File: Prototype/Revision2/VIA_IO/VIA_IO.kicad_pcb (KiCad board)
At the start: 2 copper layers, 100.2 x 88.2 mm, 88 parts, among them CN8 CONTROL_PORT, J10 VIA, J12 VIC, J18 3V3, J19 +5V, J21 JOY_POTS, J22 JOY_POTS, J23 JOY_PORT, J24 JOY_PORT, J25 SYNC, J4 KEYBOARD, J5 MOTOR, J6 9VAC, J8 EDGE, SW1 POWER_SWITCH, U1 BD60GC0WEFJ-E2, U12 THS7316D, U15 74LVC1G06, U17 74LVC1G06, U18 74LVC1G06, U19 74LVC1G06, U28 TLV74333PDBVR, U32 LM1881, U7 6522 VIA, U8 6522 VIA

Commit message: - Added the prototype rev2 IO Board schematic.
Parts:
- removed the C10 at (232.7, 81.5)
- removed the C11 at (232.7, 84.0)
- removed the C12 at (232.7, 86.5)
- removed the C35 at (126.3, 63.3)
- removed the C49 at (159.4, 55.9)
- removed the C50 at (157.6, 67.6)
- removed the C51 at (73.9, 116.6)
- removed C80: 4.7uf, Capacitor_SMD:C_0603_1608Metric
- removed C83, C84: 1nf, Capacitor_SMD:C_0603_1608Metric
- removed the C9 at (232.7, 78.9)
- removed J12: VIC, Connector_PinHeader_2.54mm:PinHeader_1x03_P2.54mm_Vertical
- removed J18: 3V3, Connector_PinHeader_2.54mm:PinHeader_1x03_P2.54mm_Vertical
- removed J19: +5V, Connector_PinHeader_2.54mm:PinHeader_2x04_P2.54mm_Vertical
- removed J21, J22: JOY_POTS, Connector_PinHeader_2.54mm:PinHeader_1x03_P2.54mm_Vertical
- removed J23, J24: JOY_PORT, Dave Footprints:JOYPORT_9PIN_HEADER
- removed J25: SYNC, Connector_PinHeader_2.54mm:PinHeader_1x04_P2.54mm_Vertical
- removed Power2: POWER, LED_SMD:LED_0805_2012Metric
- removed U19: 74LVC1G06, Package_TO_SOT_SMD:SOT-353_SC-70-5
- removed U28: TLV74333PDBVR, Package_TO_SOT_SMD:SOT-23-5
- added C1: 100nf, Capacitor_SMD:C_0603_1608Metric, F.Cu at (47.2, 101.6)
- added C16: 100nf, Capacitor_SMD:C_0603_1608Metric, F.Cu at (213.4, 56.0)
- added C17: 4.7uf, Capacitor_SMD:C_0603_1608Metric, F.Cu at (49.0, 60.9)
- added C18: 100nf, Capacitor_SMD:C_0603_1608Metric, F.Cu at (49.8, 128.6)
- added C19: 100nf, Capacitor_SMD:C_0603_1608Metric, F.Cu at (245.1, 31.8)
- added C2: 100nf, Capacitor_SMD:C_0603_1608Metric, F.Cu at (40.6, 114.1)
- added C20: 100nf, Capacitor_SMD:C_0603_1608Metric, F.Cu at (245.1, 26.8)
- added C21: 100nf, Capacitor_SMD:C_0603_1608Metric, F.Cu at (260.2, 84.9)
- added C22: 100nf, Capacitor_SMD:C_0603_1608Metric, F.Cu at (174.8, 28.9)
- added C23: 100nf, Capacitor_SMD:C_0603_1608Metric, F.Cu at (174.8, 34.0)
- added C24: 100nf, Capacitor_SMD:C_0603_1608Metric, F.Cu at (52.2, 71.0)
- added C25: 100nf, Capacitor_SMD:C_0603_1608Metric, F.Cu at (245.1, 34.3)
- added C26: 100nf, Capacitor_SMD:C_0603_1608Metric, F.Cu at (245.1, 29.3)
- added C27: 100nf, Capacitor_SMD:C_0603_1608Metric, F.Cu at (260.2, 87.4)
- added C29: 100nf, Capacitor_SMD:C_0603_1608Metric, F.Cu at (174.8, 36.5)
- added C3: 100nf, Capacitor_SMD:C_0603_1608Metric, F.Cu at (40.6, 106.6)
- added C30: 1nf, Capacitor_SMD:C_0603_1608Metric, F.Cu at (180.5, 96.1)
- added C31: 100nf, Capacitor_SMD:C_0603_1608Metric, F.Cu at (46.6, 107.8)
- added C32: 1nf, Capacitor_SMD:C_0603_1608Metric, F.Cu at (180.5, 93.6)
- added C33: 100nf, Capacitor_SMD:C_0603_1608Metric, F.Cu at (160.8, 158.4)
- added C34: 100nf, Capacitor_SMD:C_0603_1608Metric, F.Cu at (174.8, 26.4)
- added C36: 100nf, Capacitor_SMD:C_0603_1608Metric, F.Cu at (46.6, 110.3)
- added C38: 100nf, Capacitor_SMD:C_0603_1608Metric, F.Cu at (46.6, 112.8)
- added C39: 100nf, Capacitor_SMD:C_0603_1608Metric, F.Cu at (17.9, 0.72)
- added C4: 100nf, Capacitor_SMD:C_0603_1608Metric, F.Cu at (47.2, 99.1)
- added C40: 100nf, Capacitor_SMD:C_0603_1608Metric, F.Cu at (17.9, 3.23)
- added C42: 510pf, Capacitor_SMD:C_0603_1608Metric, F.Cu at (17.9, 15.8)
- added C43: 10pf, Capacitor_SMD:C_0603_1608Metric, F.Cu at (17.9, 5.75)
- added C45: 100nf, Capacitor_SMD:C_0603_1608Metric, F.Cu at (17.9, 13.3)
- added C46: 4.7uf, Capacitor_SMD:C_0603_1608Metric, F.Cu at (17.9, 10.8)
- added C48: 100nf, Capacitor_SMD:C_0603_1608Metric, F.Cu at (17.9, 8.26)
- added C5: 100nf, Capacitor_SMD:C_0603_1608Metric, F.Cu at (40.6, 111.6)
- added C54: 4.7uf, Capacitor_SMD:C_0603_1608Metric, F.Cu at (21.9, 0.72)
- added C55: 100nf, Capacitor_SMD:C_0603_1608Metric, F.Cu at (98.0, 77.5)
- added C57: 100nf, Capacitor_SMD:C_0603_1608Metric, F.Cu at (264.4, 97.9)
- added C58: 100nf, Capacitor_SMD:C_0603_1608Metric, F.Cu at (21.9, 3.23)
- added C59: 100nf, Capacitor_SMD:C_0603_1608Metric, F.Cu at (21.9, 5.75)
- added C6: 100nf, Capacitor_SMD:C_0603_1608Metric, F.Cu at (40.6, 109.1)
- added C60: 100nf, Capacitor_SMD:C_0603_1608Metric, F.Cu at (21.9, 8.26)
- added C61: 100nf, Capacitor_SMD:C_0603_1608Metric, F.Cu at (52.2, 87.6)
- added C62: 100nf, Capacitor_SMD:C_0603_1608Metric, F.Cu at (21.9, 10.8)
- added C63: 100nf, Capacitor_SMD:C_0603_1608Metric, F.Cu at (190.6, 109.0)
- added C64: 100nf, Capacitor_SMD:C_0603_1608Metric, F.Cu at (213.4, 58.5)
- added C65: 100nf, Capacitor_SMD:C_0603_1608Metric, F.Cu at (213.4, 61.0)
- added C66: 4.7uf, Capacitor_SMD:C_0603_1608Metric, F.Cu at (213.4, 63.5)
- added C67: 100nf, Capacitor_SMD:C_0603_1608Metric, F.Cu at (213.4, 66.0)
- added C68: 4.7uf, Capacitor_SMD:C_0603_1608Metric, F.Cu at (213.4, 68.5)
- added C69: 100nf, Capacitor_SMD:C_0603_1608Metric, F.Cu at (217.5, 56.0)
- added C7: 100nf, Capacitor_SMD:C_0603_1608Metric, F.Cu at (47.2, 96.6)
- added C70: 100nf, Capacitor_SMD:C_0603_1608Metric, F.Cu at (26.0, 157.0)
- added C71: 100nf, Capacitor_SMD:C_0603_1608Metric, F.Cu at (26.0, 159.5)
- added CDone1: DONE, LED_SMD:LED_0805_2012Metric, F.Cu at (200.1, 74.7)
- added D1: B140-E3, Diode_SMD:D_SOD-123, F.Cu at (161.7, 155.5)
- added D10: D_Dual_Series_ACK, Package_TO_SOT_SMD:SOT-23, F.Cu at (166.9, 80.9)
- added D2: ESDA6V1SC5, _Custom:SOT-553, B.Cu at (131.0, 136.3)
- added D4: ESDA6V1SC5, _Custom:SOT-553, F.Cu at (35.1, 179.6)
- added D5: ESDA6V1SC5, _Custom:SOT-553, F.Cu at (195.4, 75.4)
- added D6: ESDA6V1SC5, _Custom:SOT-553, F.Cu at (174.3, 121.7)
- added D7: ESDA6V1SC5, _Custom:SOT-553, F.Cu at (174.3, 124.8)
- added D8: ESDA6V1SC5, _Custom:SOT-553, F.Cu at (174.3, 128.0)
- added D9: ESDA6V1SC5, _Custom:SOT-553, F.Cu at (166.9, 77.7)
- added J1: +5V, Connector_PinHeader_2.54mm:PinHeader_2x04_P2.54mm_Vertical, F.Cu at (154.0, 156.1)
- added J10: DV INTERCONNECT, Connector_PinHeader_2.54mm:PinHeader_2x05_P2.54mm_Vertical, F.Cu at (1.79, 1.79)
- added J2: JOY_POTS, Connector_PinHeader_2.54mm:PinHeader_1x03_P2.54mm_Vertical, F.Cu at (176.2, 92.1)
- added J3: KEYBOARD, _Custom:CON_VIC20_KEYBOARD, F.Cu at (64.8, 131.8)
- added J7: USB_B_Micro, _Custom:USB_Micro-B_Amphenol_10103594-0001LF_Horizontal, F.Cu at (28.7, 177.2)
- added J9: HDMI, Connector_Video:HDMI_A_Amphenol_10029449-x01xLF_Horizontal, F.Cu at (156.5, 122.0)
- added JP1: SolderJumper_2_Bridged, Jumper:SolderJumper-2_P1.3mm_Bridged_RoundedPad1.0x1.5mm, F.Cu at (161.0, 167.0)
- added JP2: SolderJumper_2_Bridged, Jumper:SolderJumper-2_P1.3mm_Bridged_RoundedPad1.0x1.5mm, F.Cu at (254.9, 72.8)
- added Je1: BOOT SEL, Connector_PinHeader_2.54mm:PinHeader_1x02_P2.54mm_Vertical, F.Cu at (47.6, 10.3)
- added Power1: POWER, LED_SMD:LED_0805_2012Metric, F.Cu at (161.1, 163.7)
- added Q1: 2SC2712-GR,LF, Package_TO_SOT_SMD:TSOT-23, F.Cu at (102.7, 78.4)
- added R1: 1k, Resistor_SMD:R_0603_1608Metric, F.Cu at (160.8, 160.9)
- added R10: 4k7, Resistor_SMD:R_0603_1608Metric, F.Cu at (22.4, 48.5)
- added R102: 470, Resistor_SMD:R_0603_1608Metric, F.Cu at (33.9, 13.3)
- added R103: 1k, Resistor_SMD:R_0603_1608Metric, F.Cu at (33.9, 15.8)
- added R104: 1k, Resistor_SMD:R_0603_1608Metric, F.Cu at (25.9, 0.72)
- added R105: 27R, Resistor_SMD:R_0603_1608Metric, F.Cu at (21.9, 13.3)
- added R106: 27R, Resistor_SMD:R_0603_1608Metric, F.Cu at (25.9, 3.23)
- added R107: 27R, Resistor_SMD:R_0603_1608Metric, F.Cu at (21.9, 18.3)
- added R108: 27R, Resistor_SMD:R_0603_1608Metric, F.Cu at (60.6, 37.5)
- added R109: 27R, Resistor_SMD:R_0603_1608Metric, F.Cu at (98.0, 79.4)
- added R11: 4k7, Resistor_SMD:R_0603_1608Metric, F.Cu at (22.4, 51.0)
- added R110: 27R, Resistor_SMD:R_0603_1608Metric, F.Cu at (260.2, 102.5)
- added R111: 27R, Resistor_SMD:R_0603_1608Metric, F.Cu at (260.2, 100.0)
- added R112: 10k, Resistor_SMD:R_0603_1608Metric, F.Cu at (143.8, 123.7)
- added R113: 10k, Resistor_SMD:R_0603_1608Metric, F.Cu at (143.8, 125.1)
- added R114: 10k, Resistor_SMD:R_0603_1608Metric, F.Cu at (143.8, 120.8)
- added R115: 0R, Resistor_SMD:R_0603_1608Metric, F.Cu at (143.8, 122.2)
- added R116: 0R, Resistor_SMD:R_0603_1608Metric, F.Cu at (143.8, 117.8)
- added R117: 0R, Resistor_SMD:R_0603_1608Metric, F.Cu at (143.8, 119.3)
- added R118: 0R, Resistor_SMD:R_0603_1608Metric, F.Cu at (143.8, 114.9)
- added R119: 0R, Resistor_SMD:R_0603_1608Metric, F.Cu at (143.8, 116.4)
- added R12: 4k7, Resistor_SMD:R_0603_1608Metric, F.Cu at (22.4, 53.5)
- added R120: 0R, Resistor_SMD:R_0603_1608Metric, F.Cu at (217.5, 61.0)
- added R121: 0R, Resistor_SMD:R_0603_1608Metric, F.Cu at (217.5, 63.5)
- added R122: 0R, Resistor_SMD:R_0603_1608Metric, F.Cu at (21.9, 15.8)
- added R123: 0R, Resistor_SMD:R_0603_1608Metric, F.Cu at (217.5, 66.0)
- added R124: 0R, Resistor_SMD:R_0603_1608Metric, F.Cu at (26.0, 162.0)
- added R125: 0R, Resistor_SMD:R_0603_1608Metric, F.Cu at (26.0, 164.5)
- added R126: 0R, Resistor_SMD:R_0603_1608Metric, F.Cu at (26.0, 167.0)
- added R127: 0R, Resistor_SMD:R_0603_1608Metric, F.Cu at (26.0, 169.5)
- added R128: 0R, Resistor_SMD:R_0603_1608Metric, F.Cu at (26.0, 172.0)
- added R129: 0R, Resistor_SMD:R_0603_1608Metric, F.Cu at (30.0, 157.0)
- added R13: 4k7, Resistor_SMD:R_0603_1608Metric, F.Cu at (22.4, 56.0)
- added R130: 0R, Resistor_SMD:R_0603_1608Metric, F.Cu at (30.0, 159.5)
- added R131: 0R, Resistor_SMD:R_0603_1608Metric, F.Cu at (30.0, 162.0)
- added R132: 10k, Resistor_SMD:R_0603_1608Metric, F.Cu at (30.0, 164.5)
- added R133: 10k, Resistor_SMD:R_0603_1608Metric, F.Cu at (30.0, 167.0)
- added R134: 10k, Resistor_SMD:R_0603_1608Metric, F.Cu at (30.0, 169.5)
- added R135: 10k, Resistor_SMD:R_0603_1608Metric, F.Cu at (30.0, 172.0)
- added R136: 10k, Resistor_SMD:R_0603_1608Metric, F.Cu at (34.0, 157.0)
- added R137: 10k, Resistor_SMD:R_0603_1608Metric, F.Cu at (34.0, 159.5)
- added R138: 2k2, Resistor_SMD:R_0603_1608Metric, F.Cu at (34.0, 162.0)
- added R139: 220, Resistor_SMD:R_0603_1608Metric, F.Cu at (34.0, 164.5)
- added R14: 4k7, Resistor_SMD:R_0603_1608Metric, F.Cu at (22.4, 58.6)
- added R140: 220, Resistor_SMD:R_0603_1608Metric, F.Cu at (34.0, 167.0)
- added R141: 220, Resistor_SMD:R_0603_1608Metric, F.Cu at (34.0, 169.5)
- added R142: 220, Resistor_SMD:R_0603_1608Metric, F.Cu at (34.0, 172.0)
- added R143: 220, Resistor_SMD:R_0603_1608Metric, F.Cu at (38.0, 157.0)
- added R144: 220, Resistor_SMD:R_0603_1608Metric, F.Cu at (38.0, 159.5)
- added R145: 220, Resistor_SMD:R_0603_1608Metric, F.Cu at (38.0, 162.0)
- added R146: 220, Resistor_SMD:R_0603_1608Metric, F.Cu at (38.0, 164.5)
- added R147: 10k, Resistor_SMD:R_0603_1608Metric, F.Cu at (38.0, 167.0)
- added R148: 27R, Resistor_SMD:R_0603_1608Metric, F.Cu at (38.0, 169.5)
- added R15: 4k7, Resistor_SMD:R_0603_1608Metric, F.Cu at (22.4, 61.1)
- added R16: 4k7, Resistor_SMD:R_0603_1608Metric, F.Cu at (26.4, 48.5)
- added R17: 4k7, Resistor_SMD:R_0603_1608Metric, F.Cu at (26.4, 51.0)
- added R18: 4k7, Resistor_SMD:R_0603_1608Metric, F.Cu at (44.2, 76.6)
- added R19: 4k7, Resistor_SMD:R_0603_1608Metric, F.Cu at (44.2, 79.2)
- added R20: 4k7, Resistor_SMD:R_0603_1608Metric, F.Cu at (44.2, 81.7)
- added R21: 4k7, Resistor_SMD:R_0603_1608Metric, F.Cu at (60.6, 34.9)
- added R22: 4k7, Resistor_SMD:R_0603_1608Metric, F.Cu at (37.4, 76.9)
- added R23: 4k7, Resistor_SMD:R_0603_1608Metric, F.Cu at (44.2, 84.2)
- added R24: 4k7, Resistor_SMD:R_0603_1608Metric, F.Cu at (44.2, 86.7)
- added R25: 4k7, Resistor_SMD:R_0603_1608Metric, F.Cu at (44.2, 89.2)
- added R26: 4k7, Resistor_SMD:R_0603_1608Metric, F.Cu at (174.8, 41.5)
- added R27: 4k7, Resistor_SMD:R_0603_1608Metric, F.Cu at (174.8, 44.0)
- added R28: 4k7, Resistor_SMD:R_0603_1608Metric, F.Cu at (174.8, 46.5)
- added R29: 4k7, Resistor_SMD:R_0603_1608Metric, F.Cu at (178.8, 26.4)
- added R3: 4k7, Resistor_SMD:R_0603_1608Metric, F.Cu at (26.4, 56.0)
- added R30: 4k7, Resistor_SMD:R_0603_1608Metric, F.Cu at (178.8, 28.9)
- added R31: 4k7, Resistor_SMD:R_0603_1608Metric, F.Cu at (178.8, 31.5)
- added R32: 4k7, Resistor_SMD:R_0603_1608Metric, F.Cu at (178.8, 34.0)
- added R33: 4k7, Resistor_SMD:R_0603_1608Metric, F.Cu at (178.8, 36.5)
- added R34: 4k7, Resistor_SMD:R_0603_1608Metric, F.Cu at (178.8, 39.0)
- added R35: 4k7, Resistor_SMD:R_0603_1608Metric, F.Cu at (178.8, 41.5)
- added R36: 4k7, Resistor_SMD:R_0603_1608Metric, F.Cu at (178.8, 44.0)
- added R37: 4k7, Resistor_SMD:R_0603_1608Metric, F.Cu at (178.8, 46.5)
- added R4: 4k7, Resistor_SMD:R_0603_1608Metric, F.Cu at (26.4, 58.6)
- added R42: 200k, Resistor_SMD:R_0603_1608Metric, F.Cu at (245.1, 39.3)
- added R43: 200k, Resistor_SMD:R_0603_1608Metric, F.Cu at (245.1, 36.8)
- added R44: 200k, Resistor_SMD:R_0603_1608Metric, F.Cu at (260.2, 95.0)
- added R45: 200k, Resistor_SMD:R_0603_1608Metric, F.Cu at (182.8, 36.5)
- added R46: 200k, Resistor_SMD:R_0603_1608Metric, F.Cu at (182.8, 39.0)
- added R47: 10k, Resistor_SMD:R_0603_1608Metric, F.Cu at (37.4, 81.9)
- added R48: 2k2, Resistor_SMD:R_0603_1608Metric, F.Cu at (103.1, 145.1)
- added R49: 2k2, Resistor_SMD:R_0603_1608Metric, F.Cu at (138.6, 127.9)
- added R5: 4k7, Resistor_SMD:R_0603_1608Metric, F.Cu at (26.4, 61.1)
- added R50: 2k2, Resistor_SMD:R_0603_1608Metric, F.Cu at (136.5, 129.6)
- added R51: 2k2, Resistor_SMD:R_0603_1608Metric, F.Cu at (137.1, 133.7)
- added R52: 2k2, Resistor_SMD:R_0603_1608Metric, B.Cu at (129.6, 129.6)
- added R53: 2k2, Resistor_SMD:R_0603_1608Metric, B.Cu at (125.2, 131.4)
- added R54: 2k2, Resistor_SMD:R_0603_1608Metric, F.Cu at (98.0, 145.6)
- added R55: 2k2, Resistor_SMD:R_0603_1608Metric, F.Cu at (93.5, 146.5)
- added R56: 2k2, Resistor_SMD:R_0603_1608Metric, B.Cu at (121.8, 133.2)
- added R57: 2k2, Resistor_SMD:R_0603_1608Metric, B.Cu at (125.2, 132.9)
- added R58: 2k2, Resistor_SMD:R_0603_1608Metric, B.Cu at (129.6, 131.1)
- added R59: 2k2, Resistor_SMD:R_0603_1608Metric, B.Cu at (130.8, 152.4)
- added R6: 4k7, Resistor_SMD:R_0603_1608Metric, F.Cu at (30.4, 48.5)
- added R60: 2k2, Resistor_SMD:R_0603_1608Metric, B.Cu at (133.3, 152.4)
- added R61: 2k2, Resistor_SMD:R_0603_1608Metric, B.Cu at (143.8, 134.9)
- added R62: 2k2, Resistor_SMD:R_0603_1608Metric, F.Cu at (142.5, 129.3)
- added R63: 2k2, Resistor_SMD:R_0603_1608Metric, F.Cu at (144.1, 129.3)
- added R64: 2k2, Resistor_SMD:R_0603_1608Metric, F.Cu at (18.4, 48.5)
- added R65: 2k2, Resistor_SMD:R_0603_1608Metric, F.Cu at (18.4, 51.0)
- added R66: 2k2, Resistor_SMD:R_0603_1608Metric, F.Cu at (18.4, 53.5)
- added R67: 2k2, Resistor_SMD:R_0603_1608Metric, F.Cu at (60.6, 32.4)
- added R68: 2k2, Resistor_SMD:R_0603_1608Metric, F.Cu at (37.4, 79.4)
- added R69: 2k2, Resistor_SMD:R_0603_1608Metric, F.Cu at (18.4, 56.0)
- added R7: 4k7, Resistor_SMD:R_0603_1608Metric, F.Cu at (30.4, 51.0)
- added R70: 2k2, Resistor_SMD:R_0603_1608Metric, F.Cu at (18.4, 58.6)
- added R71: 2k2, Resistor_SMD:R_0603_1608Metric, F.Cu at (18.4, 61.1)
- added R72: 2k2, Resistor_SMD:R_0603_1608Metric, F.Cu at (182.8, 41.5)
- added R74: 2k2, Resistor_SMD:R_0603_1608Metric, F.Cu at (182.8, 46.5)
- added R75: 2k2, Resistor_SMD:R_0603_1608Metric, F.Cu at (186.8, 26.4)
- added R76: 2k2, Resistor_SMD:R_0603_1608Metric, F.Cu at (186.8, 28.9)
- added R77: 2k2, Resistor_SMD:R_0603_1608Metric, F.Cu at (186.8, 31.5)
- added R78: 2k2, Resistor_SMD:R_0603_1608Metric, F.Cu at (186.8, 34.0)
- added R79: 2k2, Resistor_SMD:R_0603_1608Metric, F.Cu at (186.8, 36.5)
- added R8: 4k7, Resistor_SMD:R_0603_1608Metric, F.Cu at (30.4, 53.5)
- added R80: 2k2, Resistor_SMD:R_0603_1608Metric, F.Cu at (186.8, 39.0)
- added R81: 2k2, Resistor_SMD:R_0603_1608Metric, F.Cu at (186.8, 41.5)
- added R82: 2k2, Resistor_SMD:R_0603_1608Metric, F.Cu at (186.8, 44.0)
- added R83: 2k2, Resistor_SMD:R_0603_1608Metric, F.Cu at (186.8, 46.5)
- added R84: 2k2, Resistor_SMD:R_0603_1608Metric, F.Cu at (190.8, 26.4)
- added R85: 2k2, Resistor_SMD:R_0603_1608Metric, F.Cu at (190.8, 28.9)
- added R86: 2k2, Resistor_SMD:R_0603_1608Metric, F.Cu at (190.8, 31.5)
- added R87: 2k2, Resistor_SMD:R_0603_1608Metric, F.Cu at (190.8, 34.0)
- added R88: 10k, Resistor_SMD:R_0603_1608Metric, F.Cu at (174.8, 39.0)
- added R9: 4k7, Resistor_SMD:R_0603_1608Metric, F.Cu at (30.4, 56.0)
- added R90: 1K, Resistor_SMD:R_0603_1608Metric, F.Cu at (29.9, 0.72)
- added R91: 1K, Resistor_SMD:R_0603_1608Metric, F.Cu at (33.9, 3.23)
- added R92: 620R, Resistor_SMD:R_0603_1608Metric, F.Cu at (33.9, 5.75)
- added R93: 680k, Resistor_SMD:R_0603_1608Metric, F.Cu at (33.9, 8.26)
- added R94: 75, Resistor_SMD:R_0603_1608Metric, F.Cu at (33.9, 10.8)
- added S1: RESET, Button_Switch_THT:SW_PUSH_6mm_H4.3mm, F.Cu at (37.9, 1.50)
- added TP1: TestPoint, TestPoint:TestPoint_Pad_1.0x1.0mm, F.Cu at (24.7, 86.3)
- added TP10: Luma, TestPoint:TestPoint_Pad_1.0x1.0mm, F.Cu at (21.7, 86.3)
- added TP11: TestPoint, TestPoint:TestPoint_Pad_1.0x1.0mm, F.Cu at (20.4, 37.5)
- added TP12: TestPoint, TestPoint:TestPoint_Pad_1.0x1.0mm, F.Cu at (23.5, 34.5)
- added TP13: TestPoint, TestPoint:TestPoint_Pad_1.0x1.0mm, F.Cu at (23.5, 37.5)
- added TP2: TestPoint, TestPoint:TestPoint_Pad_1.0x1.0mm, F.Cu at (24.7, 89.4)
- added TP3: TestPoint, TestPoint:TestPoint_Pad_1.0x1.0mm, F.Cu at (21.7, 77.2)
- added TP4: Composite Sync, TestPoint:TestPoint_Pad_1.0x1.0mm, F.Cu at (21.7, 89.4)
- added TP5: Vertical Sync, TestPoint:TestPoint_Pad_1.0x1.0mm, F.Cu at (24.7, 77.2)
- added TP6: Horizontal Sync, TestPoint:TestPoint_Pad_1.0x1.0mm, F.Cu at (24.7, 80.2)
- added TP7: Odd / Even, TestPoint:TestPoint_Pad_1.0x1.0mm, F.Cu at (24.7, 83.3)
- added TP8: Composite, TestPoint:TestPoint_Pad_1.0x1.0mm, F.Cu at (21.7, 80.2)
- added TP9: Chroma, TestPoint:TestPoint_Pad_1.0x1.0mm, F.Cu at (21.7, 83.3)
- added U1: ICE40HX1K-VQ100, Package_QFP:LQFP-100_14x14mm_P0.5mm, F.Cu at (96.4, 98.0)
- added U12: TLV74311PDBVR, Package_TO_SOT_SMD:SOT-23-5, F.Cu at (33.0, 35.4)
- added U13: RP2354A-QFN60, RP2350_KiCad-main:RP2350A_QFN-60_EP_7.75x7.75_Pitch0.4mm, F.Cu at (134.8, 107.6)
- added U14: ESDALD05UG4X, Package_SON:USON-10_2.5x1.0mm_P0.5mm, F.Cu at (214.0, 72.2)
- added U16: 74CBTD3861, Package_SO:SSOP-24_3.9x8.7mm_P0.635mm, F.Cu at (148.8, 76.9)
- added U2: TLV74333PDBVR, Package_TO_SOT_SMD:SOT-23-5, F.Cu at (45.1, 57.4)
- added U3: LSF0108PW, Package_SO:TSSOP-20_4.4x6.5mm_P0.65mm, F.Cu at (122.9, 117.8)
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- renumbered C4 to C10, C13 to C11, C5 to C12, C2 to C13, C6 to C14, C8 to C15, C40 to C35, C41 to C37, C42 to C41, C89 to C47, C82 to C49, C88 to C50, C1 to C8, C7 to C9, R3 to R89, U12 to U10, U32 to U11, U1 to U9
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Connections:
- net Net-(BR1-+) renamed +11.3V
- net Net-(C13-Pad1) renamed /'9VAC
- net Net-(DIN3-Pad3) renamed /SERIAL_ATTN_IO
- net Net-(DIN3-Pad4) renamed /SERIAL_CLK_IO
- net Net-(DIN3-Pad5) renamed /SERIAL_DATA_IO
- BR1 pad 3: /9VAC~ -> 9VAC~
- BR1 pad 4: /'9VAC~ -> '9VAC~
- C10 pad 1: /'9VAC~ -> '9VAC~
- C10 pad 2: /9VAC~ -> 9VAC~
- C12 pad 1: /9VAC~ -> 9VAC~
- C28 pad 2: +5V -> Net-(U6-EN)
- C35 pad 1: Net-(U12-CH.1_IN) -> +5V
- C35 pad 2: Net-(C40-Pad2) -> GND
- C37 pad 1: GND -> Net-(U10-CH.1_IN)
- C37 pad 2: +3V3 -> Net-(C37-Pad2)
- C41 pad 1: Net-(U12-CH.3_IN) -> GND
- C41 pad 2: Net-(C42-Pad2) -> Net-(U11-RSET)
- C44 pad 2: +5V -> Net-(C44-Pad2)
- C47 pad 1: Net-(C89-Pad1) -> GND
- C47 pad 2: Net-(U32-CVIN) -> +1V1
- C49 pad 2: +5V -> +1V1
- C50 pad 2: Net-(U32-RSET) -> Net-(Q1-B)
- C51 pad 2: Net-(JP3-A) -> /COMP_SOUND
- C52 pad 1: GND -> Net-(Q1-E)
- C52 pad 2: +5V -> /Audio Out
- C53 pad 1: GND -> +3V3
- C53 pad 2: +5V -> GND
- C9 pad 2: /'9VAC~ -> '9VAC~
- CN1 pad 1: /JOY0 -> /5V_9110.PA2
- CN1 pad 2: /JOY1 -> /5V_9110.PA3
- CN1 pad 3: /JOY2 -> /5V_9110.PA4
- CN1 pad 4: /JOY3 -> /5V_9120.PB7
- CN1 pad 6: /LIGHT_PEN -> /5V_9110.PA5
- D3 pad 1: Net-(D3-K) -> /5V_9110.PA2
- D3 pad 2: +5V -> GND
- DIN2 pad 1: /SERIAL_SRQ_IN -> /5V_9120.CB1
- DIN2 pad 6: /~{RES} -> /~{5V_RESET}
- EDGE1 pad C,3: /MOTOR -> /MOTOR_6VDC
- EDGE1 pad D,4: /CASS_READ -> /CASSETTE_READ
- EDGE1 pad E,5: /COL3/CASS_WRITE -> /5V_9120.PB3
- EDGE1 pad F,6: /CASSETTE_SWITCH -> /5V_9110.PA6
- EDGE2 pad 10: Net-(EDGE2-9V__AC) -> 9VAC~
- EDGE2 pad 11: Net-(EDGE2-9V_AC_) -> '9VAC~
- EDGE2 pad 3: /~{RES} -> /~{5V_RESET}
- EDGE2 pad 4: /JOY0 -> /5V_9110.PA2
- EDGE2 pad 5: /JOY1 -> /5V_9110.PA3
- EDGE2 pad 6: /JOY2 -> /5V_9110.PA4
- EDGE2 pad 7: /LIGHT_PEN -> /5V_9110.PA5
- EDGE2 pad 8: /CASSETTE_SWITCH -> /5V_9110.PA6
- EDGE2 pad B: /CB1 -> /5V_9110.CB1
- EDGE2 pad C: /PB0 -> /5V_9110.PB0
- EDGE2 pad D: /PB1 -> /5V_9110.PB1
- EDGE2 pad E: /PB2 -> /5V_9110.PB2
- EDGE2 pad F: /PB3 -> /5V_9110.PB3
- EDGE2 pad H: /PB4 -> /5V_9110.PB4
- EDGE2 pad J: /PB5 -> /5V_9110.PB5
- EDGE2 pad K: /PB6 -> /5V_9110.PB6
- EDGE2 pad L: /PB7 -> /5V_9110.PB7
- EDGE2 pad M: /CB2 -> /5V_9110.CB2
- FB2 pad 1: /SERIAL_CLK_IN -> /5V_9120.CA2
- FB3 pad 1: /SERIAL_DATA_IN -> /5V_9120.CB2
- FL1 pad 2: /9VAC~ -> 9VAC~
- FL1 pad 4: /'9VAC~ -> '9VAC~
- J10 pad 1: /CR/~{W} -> /IO.CR_~{W}
- J10 pad 10: /BD3 -> /IO.DATA3
- J10 pad 11: /BD2 -> /IO.DATA2
- J10 pad 12: /BD1 -> /IO.DATA1
- J10 pad 13: /BD0 -> /IO.DATA0
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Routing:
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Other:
- board size 100.2 x 88.2 mm -> 100 x 88.2 mm
- board text removed: "CA5"
- board text removed: "CR/~{W}"
- board text removed: "IO0"
- board text removed: "~{IRQ}"
- board text removed: "~{NMI}"

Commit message: - Initial layout of all the major components.
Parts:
- removed the C43 at (17.9, 5.75)
- removed the C46 at (17.9, 10.8)
- removed the C62 at (21.9, 10.8)
- removed the C66 at (213.4, 63.5)
- removed C71: 100nf, Capacitor_SMD:C_0603_1608Metric
- removed the D10 at (166.9, 80.9)
- removed the D5 at (195.4, 75.4)
- removed J10: DV INTERCONNECT, Connector_PinHeader_2.54mm:PinHeader_2x05_P2.54mm_Vertical
- removed the J2 at (176.2, 92.1)
- removed J6: SWD, Connector_PinHeader_2.54mm:PinHeader_1x03_P2.54mm_Vertical
- removed the J7 at (28.7, 177.2)
- removed Je1: BOOT SEL, Connector_PinHeader_2.54mm:PinHeader_1x02_P2.54mm_Vertical
- removed R100: 10k, Resistor_SMD:R_0603_1608Metric
- removed R105, R106: 27R, Resistor_SMD:R_0603_1608Metric
- removed the R114 at (143.8, 120.8)
- removed the R137 at (34.0, 159.5)
- removed the R138 at (34.0, 162.0)
- removed the R97 at (256.8, 118.0)
- removed the R98 at (256.8, 115.5)
- removed S1: RESET, Button_Switch_THT:SW_PUSH_6mm_H4.3mm
- removed U18: MIC5504-1.2YM5, Package_TO_SOT_SMD:SOT-23-5
- added AC1: 9VAC, Connector_PinHeader_2.54mm:PinHeader_1x02_P2.54mm_Vertical, F.Cu at (149.7, 134.0)
- added C51: 100nf, Capacitor_SMD:C_0603_1608Metric, B.Cu at (86.3, 99.1)
- added C52: 100nf, Capacitor_SMD:C_0603_1608Metric, B.Cu at (130.7, 99.2)
- added C64: 100nf, Capacitor_SMD:C_0603_1608Metric, B.Cu at (101.8, 94.7)
- added C68: 100nf, Capacitor_SMD:C_0603_1608Metric, B.Cu at (98.8, 100.6)
- added D12: D_Dual_Series_ACK, Package_TO_SOT_SMD:SOT-23, B.Cu at (86.5, 89.3)
- added D3: ESDALD05UG4X, Package_SON:USON-10_2.5x1.0mm_P0.5mm, F.Cu at (134.9, 135.8)
- added R102: 10k, Resistor_SMD:R_0603_1608Metric, F.Cu at (136.3, 101.4)
- added R103: 1k, Resistor_SMD:R_0603_1608Metric, F.Cu at (123.6, 101.7)
- added R112: 10k, Resistor_SMD:R_0603_1608Metric, B.Cu at (138.7, 72.1)
- added R132: 10k, Resistor_SMD:R_0603_1608Metric, F.Cu at (109.6, 97.3)
- added R133: 2k2, Resistor_SMD:R_0603_1608Metric, F.Cu at (109.6, 98.8)
- added U16: MIC5504-1.2YM5, Package_TO_SOT_SMD:SOT-23-5, B.Cu at (91.8, 99.4)
- C1, C2, C3, C39, C4, C47, C49, C5, C53, C55, C56, C57, C58, C59, C6, C60, C67, C69, C7, C70, D9, FB1, FB2, FB3, JP1, JP3, JP4, R113, R115, R116, R117, R118, R119, R120, R121, R122, R123, R124, R125, R126, R127, R128, R129, R130, R131, R147, R72, R73, R74, R75, R76, R77, R78, R79, R80, R81, R82, R83, R84, R85, R86, R87: moved to B.Cu
- C30: renamed from C32; moved to B.Cu
- C31: renamed from C30; moved to B.Cu
- C36: renamed from C52; moved to B.Cu
- C45: value 100nf -> 10pf
- C48, C65: value 100nf -> 4.7uf; moved to B.Cu
- D2: moved to F.Cu
- D4: renamed from D3; moved to F.Cu
- D6: value ESDA6V1SC5 -> ESDALD05UG4X; footprint _Custom:SOT-553 -> Package_SON:USON-10_2.5x1.0mm_P0.5mm
- D7, D8: value ESDA6V1SC5 -> ESDALD05UG4X; footprint _Custom:SOT-553 -> Package_SON:USON-10_2.5x1.0mm_P0.5mm; moved to B.Cu
- J1: footprint Connector_PinHeader_2.54mm:PinHeader_2x04_P2.54mm_Vertical -> Connector_PinHeader_2.54mm:PinHeader_2x03_P2.54mm_Vertical
- J4: footprint Connector_PinHeader_2.54mm:PinHeader_1x04_P2.54mm_Vertical -> Connector_PinHeader_2.54mm:PinHeader_1x08_P2.54mm_Vertical
- J5: value AV INPUT -> SWD; footprint Connector_PinHeader_2.54mm:PinHeader_1x04_P2.54mm_Vertical -> Connector_PinHeader_2.54mm:PinHeader_1x03_P2.54mm_Vertical
- R10, R11, R12, R13, R14, R15, R16, R17, R18, R19, R2, R20, R21, R22, R23, R24, R25, R26, R27, R28, R29, R3, R30, R31, R32, R33, R34, R35, R36, R37, R38, R39, R4, R40, R41, R48, R49, R5, R50, R51, R54, R55, R6, R62, R63, R64, R65, R66, R67, R68, R69, R7, R70, R71, R8, R9: footprint Resistor_SMD:R_0603_1608Metric -> Resistor_SMD:R_0402_1005Metric
- R101: value 1k -> 27R; moved to B.Cu
- R104: renamed from R89; value 220 -> 220R
- R114: renamed from R112; moved to B.Cu
- R52, R53, R56, R57, R58, R59, R60, R61: footprint Resistor_SMD:R_0603_1608Metric -> Resistor_SMD:R_0402_1005Metric; moved to F.Cu
- R88: renamed from R102; value 470 -> 470R
- R90: renamed from R88; moved to B.Cu
- R92: renamed from R94; value 75 -> 75R; moved to B.Cu
- R93: renamed from R95; value 75 -> 75R
- R94: renamed from R96; value 75 -> 75R
- R99: value 27R -> 10k; moved to B.Cu
- U1: value ICE40HX1K-VQ100 -> iCE40HX1K-VQ100
- moved R93 216.1 mm to (38.5, 90.6)
- moved R94 214.6 mm to (42.5, 78.1)
- moved C34 180.1 mm to (75.0, 75.9), turned to 180 degrees
- moved C35 176.4 mm to (80.0, 77.7), turned to 180 degrees
- moved R135 175.0 mm to (165.2, 60.8)
- moved R134 171.9 mm to (165.2, 63.3)
- moved R136 171.9 mm to (165.2, 58.3)
- moved TP11 169.1 mm to (172.5, 111.6)
- moved TP12 169.1 mm to (175.5, 108.5)
- moved TP13 169.1 mm to (175.5, 111.6)
- moved C43 162.9 mm to (88.7, 83.1), turned to 180 degrees
- moved C27 160.5 mm to (103.6, 122.8), turned to -90 degrees
- moved C21 160.1 mm to (103.6, 118.6), turned to -90 degrees
- moved R44 158.9 mm to (104.3, 125.8), turned to -90 degrees
- moved C26 157.8 mm to (117.8, 122.7), turned to -90 degrees
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- renumbered C31 to C32, C50 to C34, C51 to C35, C35 to C37, C42 to C38, C41 to C40, C40 to C41, C38 to C42, C37 to C43, C36 to C46, C34 to C50, C63 to C62, C64 to C63, C68 to C66, U14 to D10, U15 to D11, D4 to D5, J3 to J2, J5 to J3, J8 to J7, J9 to J8, J10 to J9, R132 to R136, R133 to R137, R136 to R138, R103 to R89, R104 to R91, R92 to R95, R93 to R96, R91 to R97, R90 to R98, RV2 to RV1, RV1 to RV2, TP7 to TP10, TP8 to TP4, TP9 to TP5, TP10 to TP6, TP4 to TP7, TP5 to TP8, TP6 to TP9, U11 to U10, U10 to U11, U16 to U14, U17 to U15
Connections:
- net /Audio Out renamed /AUDIO OUT
- BR1 pad 3: 9VAC~ -> 9VAC22
- BR1 pad 4: '9VAC~ -> '9VAC22
- C10 pad 1: '9VAC~ -> '9VAC22
- C10 pad 2: 9VAC~ -> 9VAC22
- C12 pad 1: 9VAC~ -> 9VAC22
- C30 pad 1: /POT_Y -> POT_Y
- C31 pad 1: /POT_X -> POT_X
- C44 pad 2: Net-(C44-Pad2) -> Net-(U13-XIN)
- C45 pad 2: +1V1 -> Net-(C45-Pad2)
- C48 pad 1: +3V3 -> GND
- C48 pad 2: GND -> Net-(U13-VREG_AVDD)
- C65 pad 2: +3V3 -> +1V2
- C9 pad 2: '9VAC~ -> '9VAC22
- CN1 pad 5: /POT_Y -> POT_Y
- CN1 pad 9: /POT_X -> POT_X
- D2 pad 1: /5V_9110.PA6 -> +5V
- D2 pad 3: /5V_9120.PB3 -> /CASSETTE_READ
- D2 pad 4: /CASSETTE_READ -> /5V_9120.PB3
- D2 pad 5: +5V -> /5V_9110.PA6
- D4 pad 3: /POT_Y -> POT_Y
- D4 pad 4: /POT_X -> POT_X
- D6 pad 1: /5V_9110.PB0 -> /5V_9110.PA2
- D6 pad 2: GND -> /5V_9110.PB0
- D6 pad 3: /5V_9110.CB1 -> GND
- D6 pad 5: /5V_9110.PA2 -> /5V_9110.CB1
- D7 pad 1: /5V_9110.PB4 -> /5V_9110.PB1
- D7 pad 2: GND -> /5V_9110.PB2
- D7 pad 3: /5V_9110.PB3 -> GND
- D7 pad 4: /5V_9110.PB2 -> /5V_9110.PB3
- D7 pad 5: /5V_9110.PB1 -> /5V_9110.PB4
- D8 pad 1: /5V_9110.CB2 -> /5V_9110.PB5
- D8 pad 2: GND -> /5V_9110.PB6
- D8 pad 3: /5V_9110.PB7 -> GND
- D8 pad 4: /5V_9110.PB6 -> /5V_9110.PB7
- D8 pad 5: /5V_9110.PB5 -> /5V_9110.CB2
- D9 pad 1: /5V_9120.CB1 -> /SERIAL_ATTN_IO
- D9 pad 3: /SERIAL_ATTN_IO -> /5V_9120.CB1
- D9 pad 4: /SERIAL_CLK_IO -> /SERIAL_DATA_IO
- D9 pad 5: /SERIAL_DATA_IO -> /SERIAL_CLK_IO
- EDGE2 pad 10: 9VAC~ -> /9VAC~
- EDGE2 pad 11: '9VAC~ -> /~{9VAC~}
- FL1 pad 2: 9VAC~ -> 9VAC22
- FL1 pad 4: '9VAC~ -> '9VAC22
- J4 pad 1: /COMP_COLOUR -> /5V_9110.PA5
- J4 pad 2: /SYNC_LUMA -> /COMP_SOUND
- J4 pad 3: /COMP_SOUND -> /EXT_AUDIO_IN
- J4 pad 4: /EXT_AUDIO_IN -> POT_Y
- J5 pad 1: /COMP_COLOUR -> /2354_SWCLK
- J5 pad 2: /SYNC_LUMA -> GND
- J5 pad 3: /COMP_SOUND -> /2354_SWDIO
- R101 pad 1: Net-(C44-Pad2) -> +3V3
- R101 pad 2: Net-(U13-XOUT) -> Net-(U13-VREG_AVDD)
- R113 pad 1: Net-(U17-B9) -> Net-(U14-B9)
- R134 pad 1: Net-(U17-A9) -> Net-(U14-A8)
- R135 pad 1: Net-(U17-A10) -> Net-(U14-A9)
- R99 pad 2: Net-(U13-VREG_AVDD) -> Net-(U13-RUN)
- U1 pad 26: /3V3_9110.CA2 -> /3V3_9120.~{IRQ}
- U1 pad 27: /3V3_9110.CB2 -> /3V3_9120.CB2
- U1 pad 28: /3V3_9110.~{NMI} -> /3V3_9120.CA2
- U1 pad 29: /3V3_9110.CA1 -> /3V3_9120.CB1
- U1 pad 30: /3V3_9110.CB1 -> /3V3_9120.CA1
- U1 pad 36: /3V3_9120.CA1 -> /3V3_9110.CB1
- U1 pad 37: /3V3_9120.CB1 -> /3V3_9110.CA1
- U1 pad 40: /3V3_9120.CA2 -> /3V3_9110.~{NMI}
- U1 pad 41: /3V3_9120.CB2 -> /3V3_9110.CB2
- U1 pad 42: /3V3_9120.~{IRQ} -> /3V3_9110.CA2
- U14 pad 10: /IO.CR_~{W} -> Net-(U14-A9)
- U14 pad 14: /3V3.CR_~{W} -> Net-(U14-B9)
- U14 pad 15: /3V3.IO0 -> Net-(U14-B8)
- U14 pad 16: /3V3.SO2 -> /3V3.ADDRESS0
- U14 pad 17: /3V3.ADDRESS5 -> /3V3.ADDRESS1
- U14 pad 18: /3V3.ADDRESS4 -> /3V3.ADDRESS2
- U14 pad 2: /IO.ADDRESS0 -> /IO.SO2
- U14 pad 20: /3V3.ADDRESS2 -> /3V3.ADDRESS4
- U14 pad 21: /3V3.ADDRESS1 -> /3V3.ADDRESS5
- U14 pad 22: /3V3.ADDRESS0 -> /3V3.SO2
- U14 pad 3: /IO.ADDRESS1 -> /IO.ADDRESS5
- U14 pad 4: /IO.ADDRESS2 -> /IO.ADDRESS4
- U14 pad 6: /IO.ADDRESS4 -> /IO.ADDRESS2
- U14 pad 7: /IO.ADDRESS5 -> /IO.ADDRESS1
- U14 pad 8: /IO.SO2 -> /IO.ADDRESS0
- U14 pad 9: /IO.IO0 -> Net-(U14-A8)
- U15 pad 10: Net-(U17-A9) -> /IO.DATA1
- U15 pad 11: Net-(U17-A10) -> /IO.DATA0
- U15 pad 13: Net-(U17-B10) -> /3V3.DATA0
- U15 pad 14: Net-(U17-B9) -> /3V3.DATA1
- U15 pad 15: /3V3.DATA7 -> /3V3.DATA2
- U15 pad 16: /3V3.DATA6 -> /3V3.DATA3
- U15 pad 17: /3V3.DATA5 -> /3V3.DATA4
- U15 pad 18: /3V3.DATA4 -> /3V3.DATA5
- U15 pad 19: /3V3.DATA3 -> /3V3.DATA6
- U15 pad 2: /IO.DATA0 -> /IO.CR_~{W}
- U15 pad 20: /3V3.DATA2 -> /3V3.DATA7
- U15 pad 21: /3V3.DATA1 -> /3V3.IO0
- U15 pad 22: /3V3.DATA0 -> /3V3.CR_~{W}
- U15 pad 3: /IO.DATA1 -> /IO.IO0
- U15 pad 4: /IO.DATA2 -> /IO.DATA7
- U15 pad 5: /IO.DATA3 -> /IO.DATA6
- U15 pad 6: /IO.DATA4 -> /IO.DATA5
- U15 pad 7: /IO.DATA5 -> /IO.DATA4
- U15 pad 8: /IO.DATA6 -> /IO.DATA3
- U15 pad 9: /IO.DATA7 -> /IO.DATA2
- Y1 pad 3: Net-(C44-Pad2) -> Net-(C45-Pad2)
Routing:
- net +3V3: track 0.00 -> 300.7 mm, vias 0 -> 61
- net GND: track 21.3 -> 162.2 mm, vias 4 -> 82
- net +5V: track 1.55 -> 133.9 mm, vias 0 -> 29
- net +1V2: track 0.00 -> 33.3 mm, vias 0 -> 4
- net /5V_9110.PA6: track 10.2 -> 40.1 mm
- net +1V1: track 0.00 -> 24.7 mm, vias 0 -> 4
- net /5V_9110.PA3: track 0.00 -> 24.0 mm
- net /2354_SWCLK: track 0.00 -> 22.2 mm
- net /IO.DATA0: track 0.00 -> 21.4 mm, vias 0 -> 1
- net /IO.DATA1: track 0.00 -> 19.7 mm, vias 0 -> 1
- net /5V_9110.PA7: track 0.00 -> 19.4 mm
- net /IO.DATA2: track 0.00 -> 17.8 mm, vias 0 -> 1
- net /5V_9110.CB1: track 0.00 -> 17.7 mm, vias 0 -> 1
- net /MOTOR_6VDC: track 0.00 -> 17.6 mm, vias 0 -> 2
- net /IO.DATA3: track 0.00 -> 15.8 mm, vias 0 -> 1
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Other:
- board text added: "BD0"
- board text added: "BD1"
- board text added: "BD2"
- board text added: "BD3"
- board text added: "BD4"
- board text added: "BD5"
- board text added: "BD6"
- board text added: "BD7"
- board text added: "CA1"
- board text added: "CA2"
- board text added: "CA3"
- board text added: "CA4"
- board text added: "CA5"
- board text added: "COLOUR"
- board text added: "CR/~{W}"
- board text added: "EX SND"
- board text added: "IO0"
- board text added: "LUMA"
- board text added: "Level Shift Bypass"
- board text added: "PEN"
- board text added: "POT X"
- board text added: "POT Y"
- board text added: "S02"
- board text added: "SOUND"
- board text added: "~{IRQ}"
- board text added: "~{NMI}"
- board text added: "~{RST}"

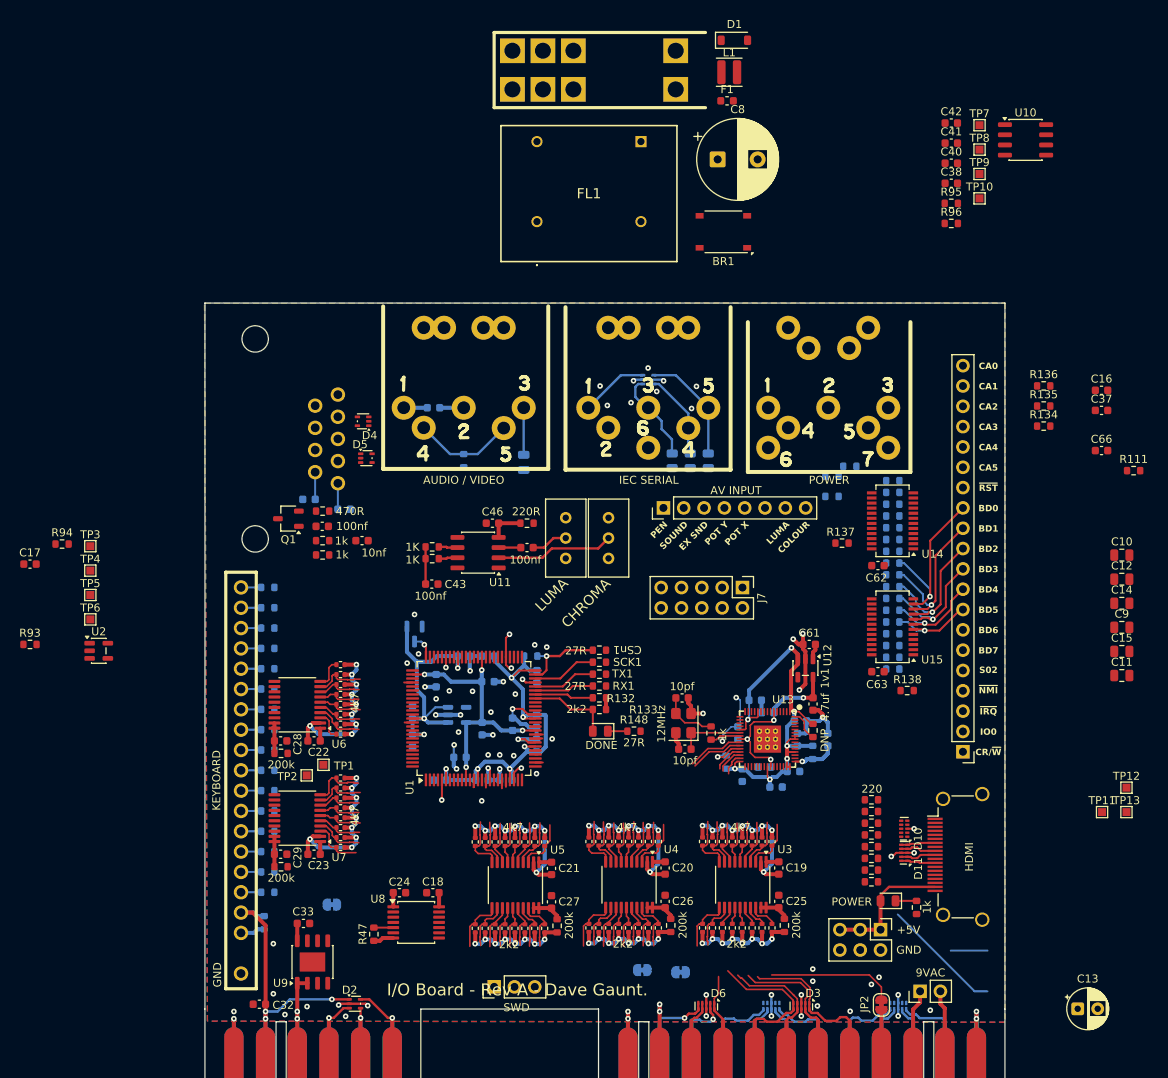
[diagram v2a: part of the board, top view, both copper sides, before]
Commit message: - Reorganised the prototype IO board layout for easier routing.
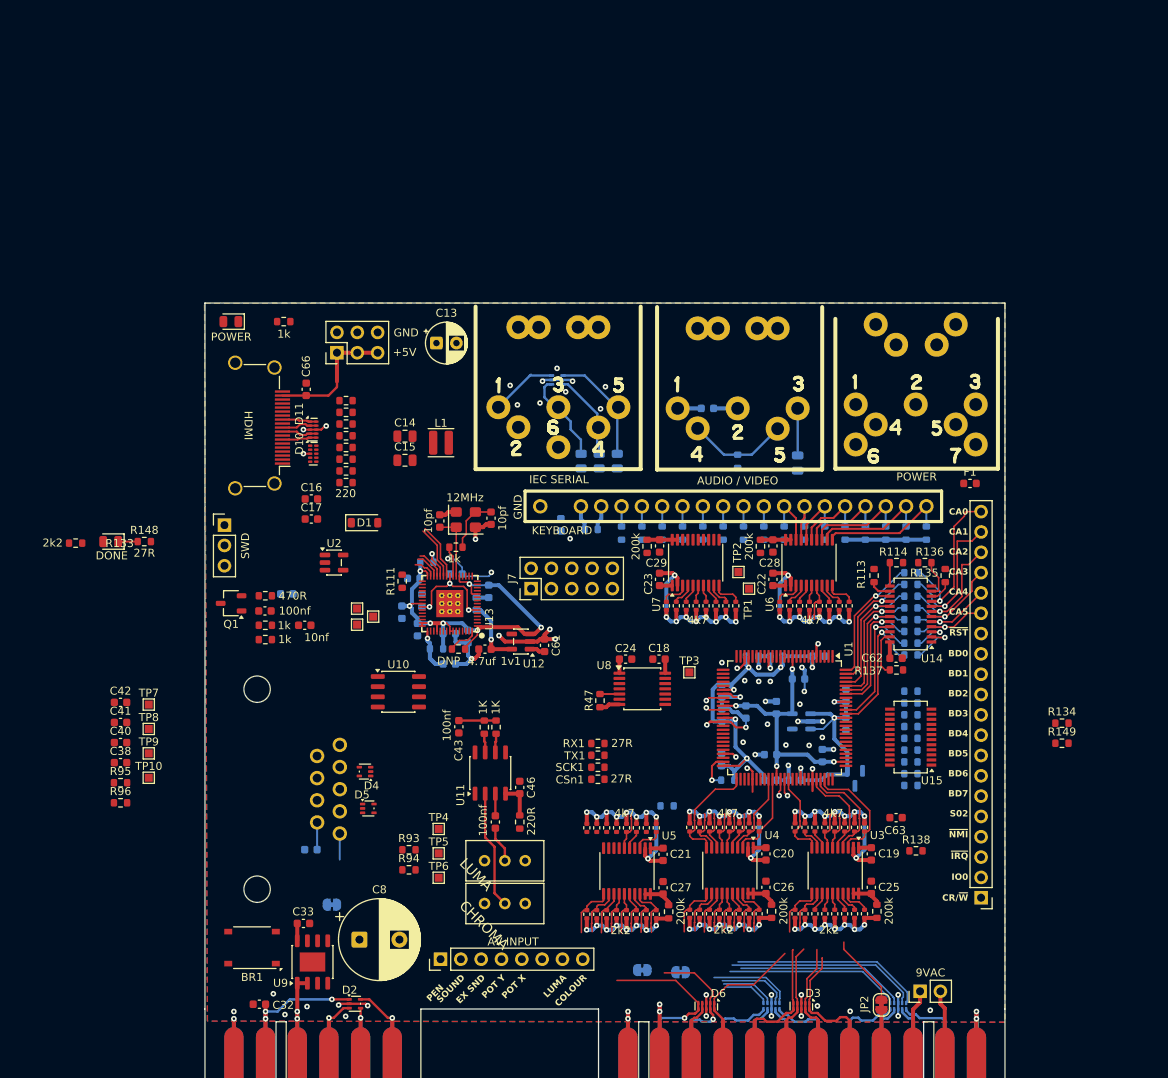
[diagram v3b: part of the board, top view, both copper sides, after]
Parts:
- removed C10, C11, C12, C9: 220nf, Capacitor_SMD:C_0805_2012Metric
- removed FL1: 2.7mH 2.2A Choke, _Custom:CHOKE_SSHB10HSR22027
- removed R112: 10k, Resistor_SMD:R_0603_1608Metric
- removed SW1: POWER_SWITCH, _Custom:SWITCH_C64_POWER
- added R149: 10k, Resistor_SMD:R_0603_1608Metric, F.Cu at (167.4, 103.0)
- C37, R132: moved to B.Cu
- R113, R114: moved to F.Cu
- moved TP10 126.6 mm to (53.3, 107.3)
- moved C38 126.6 mm to (49.8, 105.4)
- moved TP7 126.6 mm to (53.3, 98.1)
- moved TP8 126.6 mm to (53.3, 101.2)
- moved TP9 126.6 mm to (53.3, 104.2)
- moved C40 126.6 mm to (49.8, 102.9)
- moved C41 126.6 mm to (49.8, 100.4)
- moved C42 126.6 mm to (49.8, 97.9)
- moved R95 126.6 mm to (49.8, 107.9)
- moved R96 126.6 mm to (49.8, 110.4)
- moved C13 115.5 mm to (89.3, 53.0)
- moved Power1 109.5 mm to (63.6, 50.3)
- moved R1 107.8 mm to (70.2, 50.3), turned to 180 degrees
- moved C8 107.3 mm to (79.6, 127.5)
- moved BR1 107.1 mm to (66.2, 128.5)
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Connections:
- R121 pad 1: /IO.SO2 -> /IO.IO0
- R121 pad 2: /3V3.SO2 -> /3V3.IO0
- R122 pad 1: /IO.IO0 -> /IO.SO2
- R122 pad 2: /3V3.IO0 -> /3V3.SO2
- R134 pad 1: Net-(U14-A8) -> GND
- R134 pad 2: GND -> Net-(U15-B1)
- U1 pad 100: unconnected-(U1A-IOT_95-Pad100) -> /3V3.ADDRESS0
- U1 pad 26: /3V3_9120.~{IRQ} -> /3V3_9120.CA1
- U1 pad 27: /3V3_9120.CB2 -> /3V3_9120.~{IRQ}
- U1 pad 28: /3V3_9120.CA2 -> /3V3_9120.CB2
- U1 pad 30: /3V3_9120.CA1 -> /3V3_9120.CA2
- U1 pad 36: /3V3_9110.CB1 -> /3V3_9110.CA1
- U1 pad 37: /3V3_9110.CA1 -> /3V3_9110.~{NMI}
- U1 pad 40: /3V3_9110.~{NMI} -> /3V3_9110.CB2
- U1 pad 41: /3V3_9110.CB2 -> /3V3_9110.CB1
- U1 pad 78: /3V3.ADDRESS0 -> /3V3.DATA7
- U1 pad 79: /3V3.ADDRESS1 -> /3V3.DATA6
- U1 pad 80: /3V3.ADDRESS2 -> /3V3.DATA5
- U1 pad 81: /3V3.ADDRESS3 -> /3V3.DATA4
- U1 pad 82: /3V3.ADDRESS4 -> /3V3.DATA3
- U1 pad 83: /3V3.ADDRESS5 -> /3V3.DATA2
- U1 pad 85: /3V3.DATA0 -> /3V3.DATA1
- U1 pad 86: /3V3.DATA1 -> /3V3.DATA0
- U1 pad 87: /3V3.DATA2 -> unconnected-(U1A-IOT_82-Pad87)
- U1 pad 91: /3V3.DATA3 -> unconnected-(U1A-IOT_86-Pad91)
- U1 pad 93: /3V3.DATA4 -> unconnected-(U1A-IOT_87-Pad93)
- U1 pad 94: /3V3.DATA5 -> /3V3.ADDRESS5
- U1 pad 95: /3V3.DATA6 -> /3V3.ADDRESS4
- U1 pad 96: /3V3.DATA7 -> /3V3.ADDRESS3
- U1 pad 97: unconnected-(U1A-IOT_91-Pad97) -> /3V3.ADDRESS2
- U1 pad 99: unconnected-(U1A-IOT_93-Pad99) -> /3V3.ADDRESS1
- U14 pad 15: Net-(U14-B8) -> /3V3.ADDRESS0
- U14 pad 16: /3V3.ADDRESS0 -> /3V3.ADDRESS1
- U14 pad 17: /3V3.ADDRESS1 -> /3V3.ADDRESS2
- U14 pad 18: /3V3.ADDRESS2 -> /3V3.ADDRESS3
- U14 pad 19: /3V3.ADDRESS3 -> /3V3.ADDRESS4
- U14 pad 2: /IO.SO2 -> /IO.CR_~{W}
- U14 pad 20: /3V3.ADDRESS4 -> /3V3.ADDRESS5
- U14 pad 21: /3V3.ADDRESS5 -> /3V3.IO0
- U14 pad 22: /3V3.SO2 -> /3V3.CR_~{W}
- U14 pad 3: /IO.ADDRESS5 -> /IO.IO0
- U14 pad 4: /IO.ADDRESS4 -> /IO.ADDRESS5
- U14 pad 5: /IO.ADDRESS3 -> /IO.ADDRESS4
- U14 pad 6: /IO.ADDRESS2 -> /IO.ADDRESS3
- U14 pad 7: /IO.ADDRESS1 -> /IO.ADDRESS2
- U14 pad 8: /IO.ADDRESS0 -> /IO.ADDRESS1
- U14 pad 9: Net-(U14-A8) -> /IO.ADDRESS0
- U15 pad 2: /IO.CR_~{W} -> Net-(U15-A1)
- U15 pad 21: /3V3.IO0 -> /3V3.SO2
- U15 pad 22: /3V3.CR_~{W} -> Net-(U15-B1)
- U15 pad 3: /IO.IO0 -> /IO.SO2
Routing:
- net /5V_9110.PB7: track 14.2 -> 38.4 mm
- net /5V_9110.CB2: track 16.3 -> 40.4 mm
- net /5V_9110.PB5: track 16.8 -> 38.7 mm
- net /IO.DATA0: track 21.4 -> 0.00 mm, vias 1 -> 0
- net /5V_9110.PB6: track 13.8 -> 35.1 mm
- net /IO.ADDRESS0: track 0.00 -> 20.7 mm, vias 0 -> 1
- net /IO.DATA1: track 19.7 -> 0.00 mm, vias 1 -> 0
- net /IO.ADDRESS1: track 0.00 -> 18.9 mm, vias 0 -> 1
- net /3V3.IO0: track 0.00 -> 18.8 mm, vias 0 -> 1
- net /3V3.ADDRESS0: track 0.00 -> 17.8 mm, vias 0 -> 1
- net /IO.DATA2: track 17.8 -> 0.00 mm, vias 1 -> 0
- net /3V3.ADDRESS2: track 0.00 -> 17.6 mm, vias 0 -> 1
- net /3V3.ADDRESS4: track 0.00 -> 17.4 mm, vias 0 -> 1
- net /3V3.CR_~{W}: track 0.99 -> 18.4 mm, vias 0 -> 1
- net /3V3.ADDRESS5: track 0.00 -> 17.0 mm, vias 0 -> 1
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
